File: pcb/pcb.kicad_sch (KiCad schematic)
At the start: 47 parts, among them J1 BATT, J2 BATT, SW1 SW_SPST, SW10 SW_SPST, SW11 SW_SPST, SW13 SW_SPST, SW14 SW_SPST, SW15 SW_SPST, SW16 SW_SPST, SW17 SW_SPST, SW19 SW_SPST, SW2 SW_SPST, SW20 SW_SPST, SW21 SW_SPST, SW3 SW_SPST, SW4 SW_SPST, SW5 SW_SPST, SW7 SW_SPST, SW8 SW_SPST, SW9 SW_SPST, U1 XIAO_nRF52840

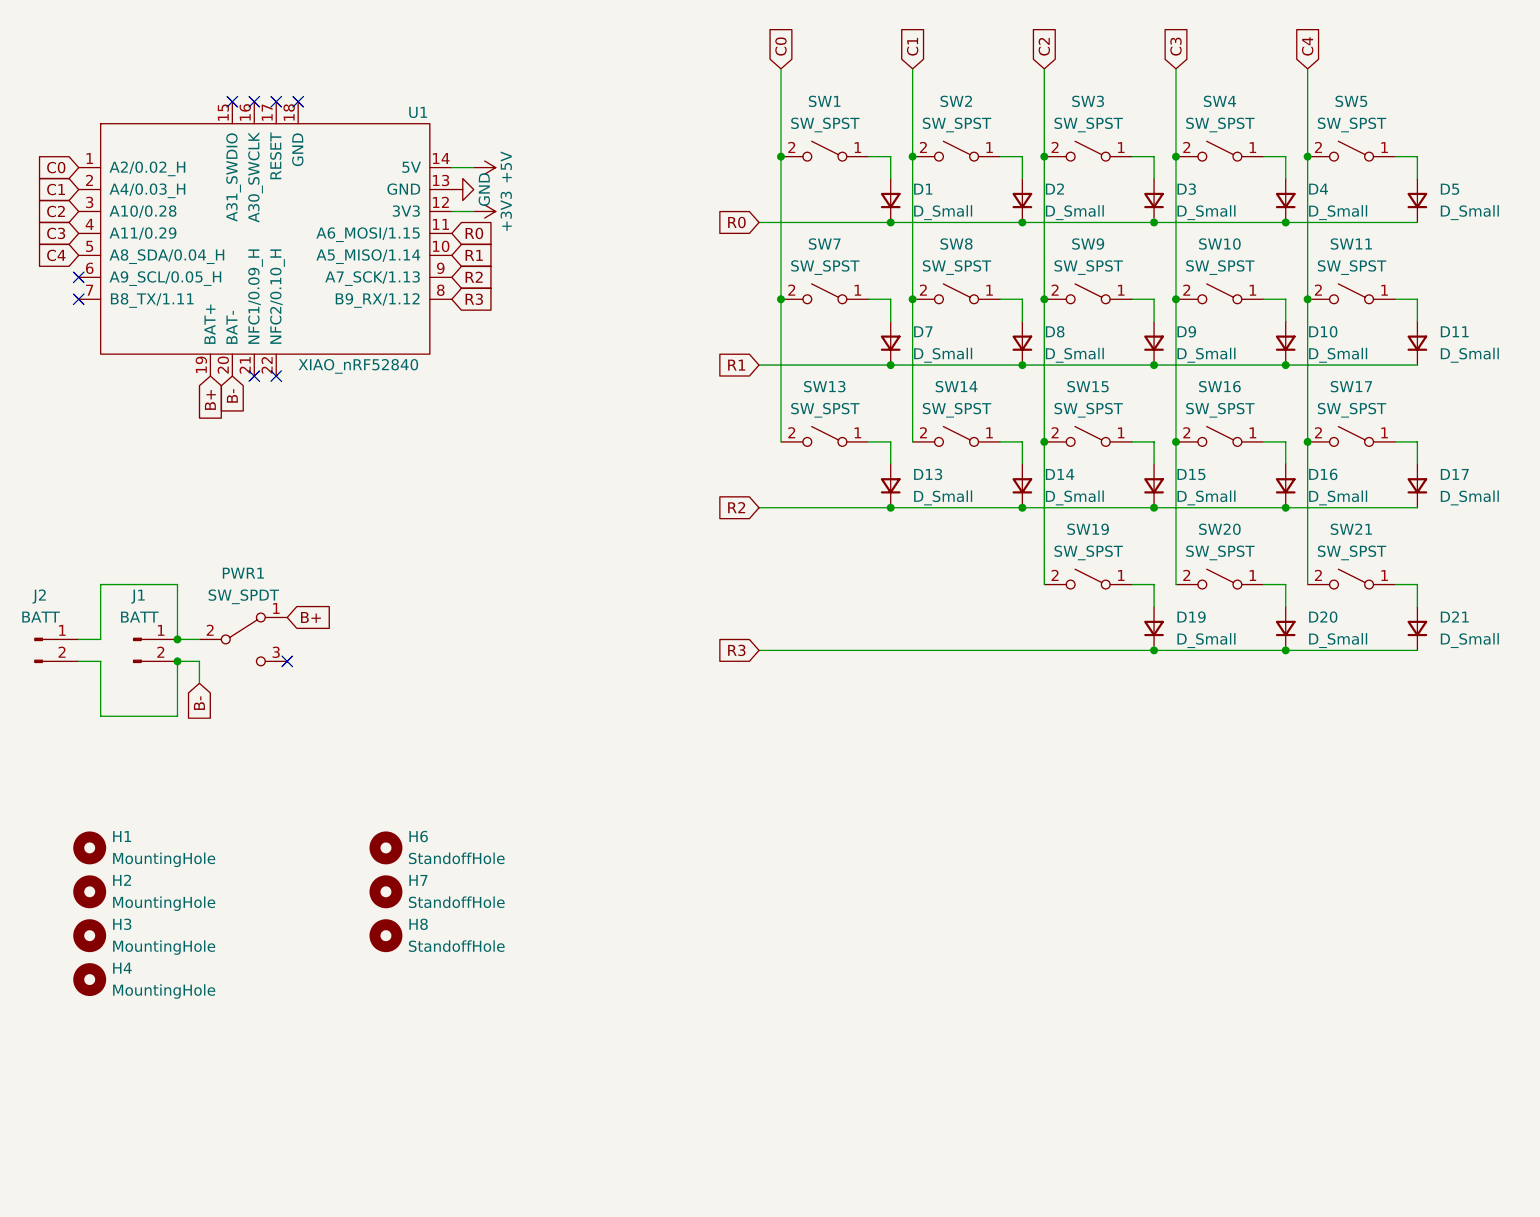
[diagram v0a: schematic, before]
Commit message: fix: symbol references
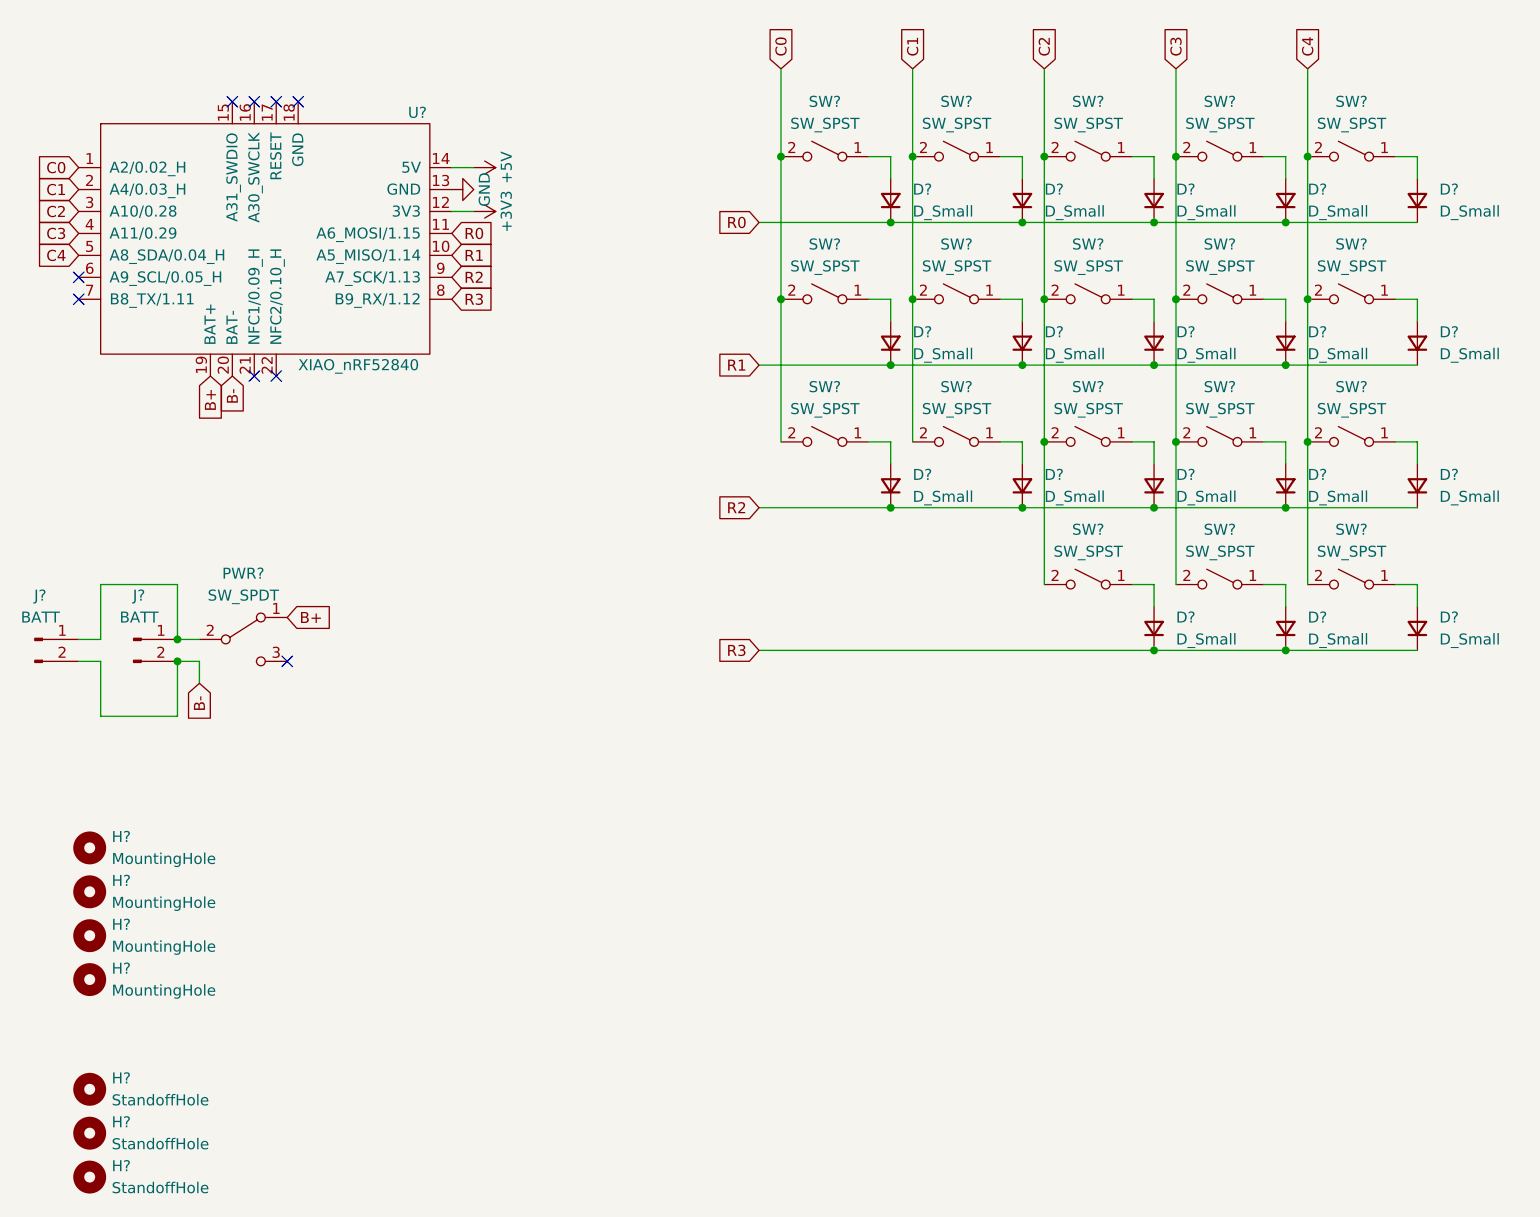
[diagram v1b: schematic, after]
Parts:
- renumbered D2 to D?, D19 to D?, D3 to D?, D13 to D?, D1 to D?, D4 to D?, D11 to D?, D7 to D?, D9 to D?, D16 to D?, D21 to D?, D8 to D?, D17 to D?, D15 to D?, D20 to D?, D10 to D?, D5 to D?, D14 to D?, H4 to H?, H6 to H?, H2 to H?, H3 to H?, H7 to H?, H1 to H?, H8 to H?, J1 to J?, J2 to J?, PWR1 to PWR?, SW17 to SW?, SW15 to SW?, SW9 to SW?, SW2 to SW?, SW21 to SW?, SW14 to SW?, SW3 to SW?, SW1 to SW?, SW11 to SW?, SW16 to SW?, SW7 to SW?, SW4 to SW?, SW8 to SW?, SW19 to SW?, SW13 to SW?, SW10 to SW?, SW20 to SW?, SW5 to SW?, U1 to U?
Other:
- moved on the sheet: H?

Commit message: add ci and 3d files
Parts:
- D? (x18): footprint scuffy:Diode_TH_SMD_DUAL -> one-s:Diode_TH_SMD_DUAL
- H? (x4): footprint scuffy:Hole_4.2mm -> one-s:Hole_4.2mm
- H? (x3): footprint scuffy:Hole_2.2mm -> one-s:Hole_2.2mm
- J?: footprint scuffy:Battery -> one-s:Battery
- J?: footprint scuffy:JST_SH_Battery_DUAL -> one-s:JST_SH_Battery_DUAL
- PWR?: footprint scuffy:MSK-12C02_DUAL -> one-s:MSK-12C02_DUAL
- SW? (x18): footprint scuffy:KS-27_KS-33_Hotswap_1U_DUAL -> one-s:KS-27_KS-33_Hotswap_1U_DUAL
- U?: footprint scuffy:XIAO_nRF52840_DUAL -> one-s:XIAO_nRF52840_DUAL

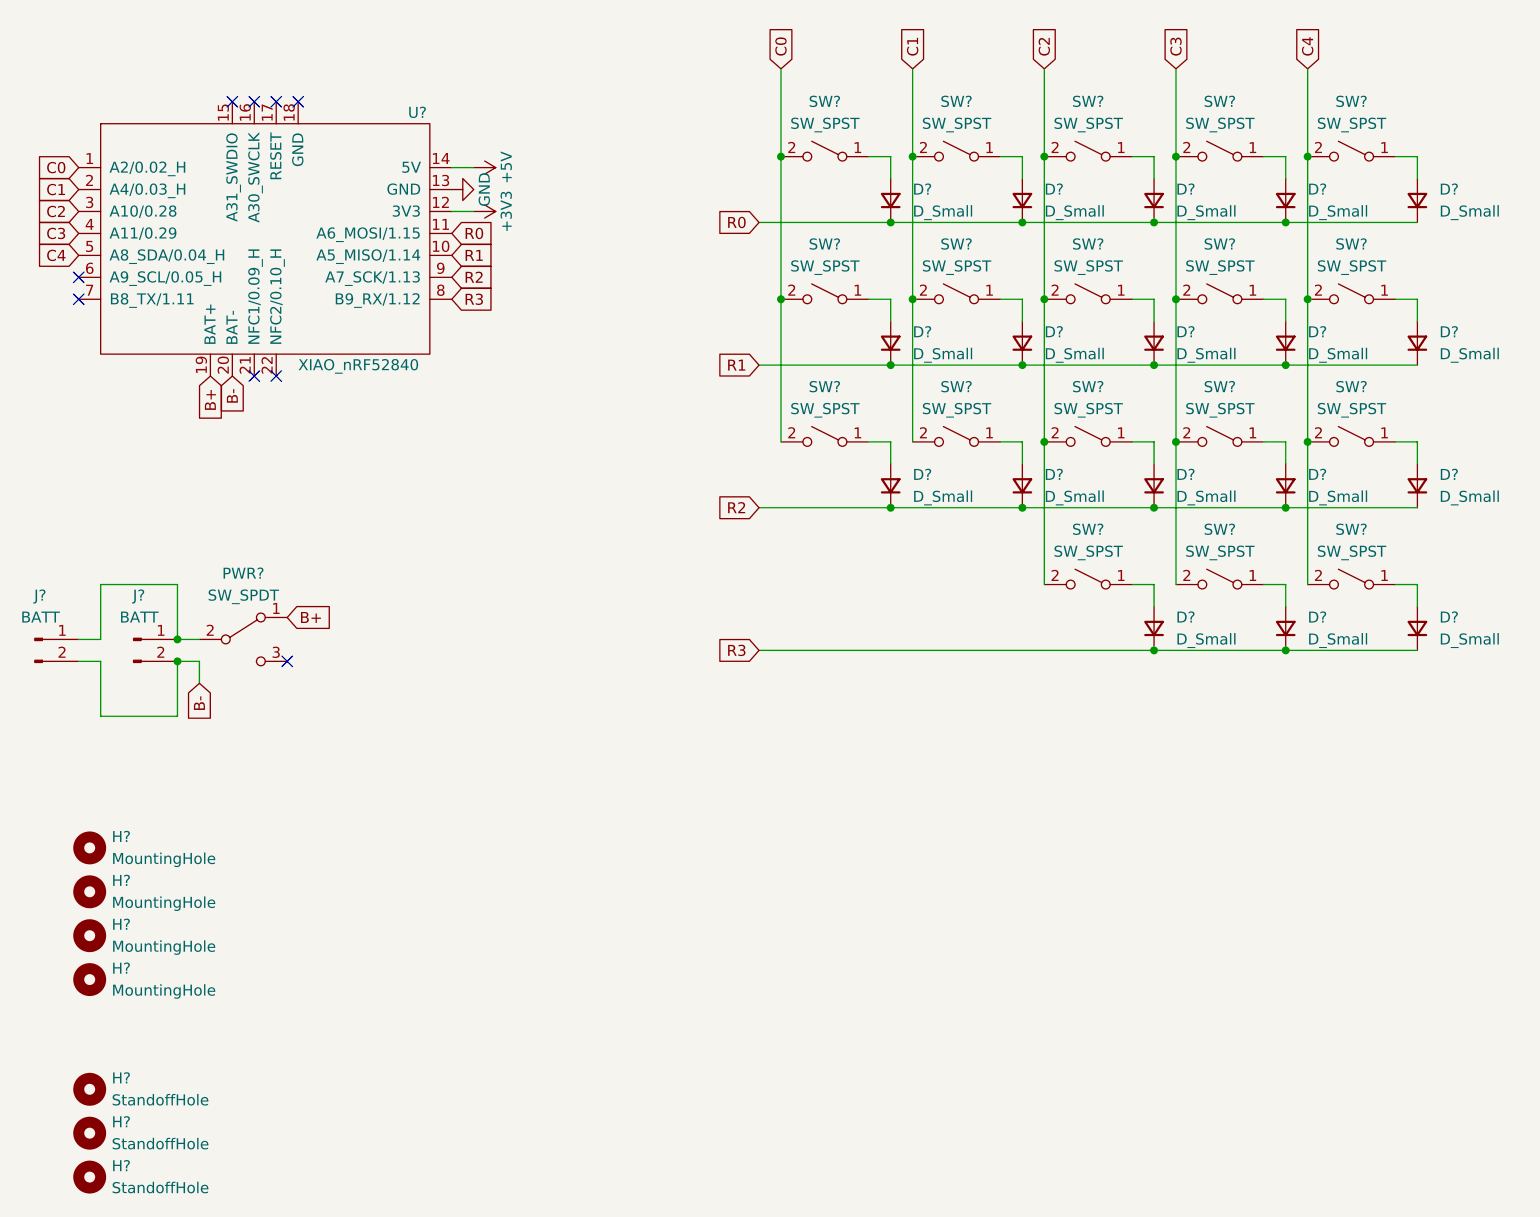
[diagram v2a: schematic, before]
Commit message: Modify PCB for Kailh P1316S
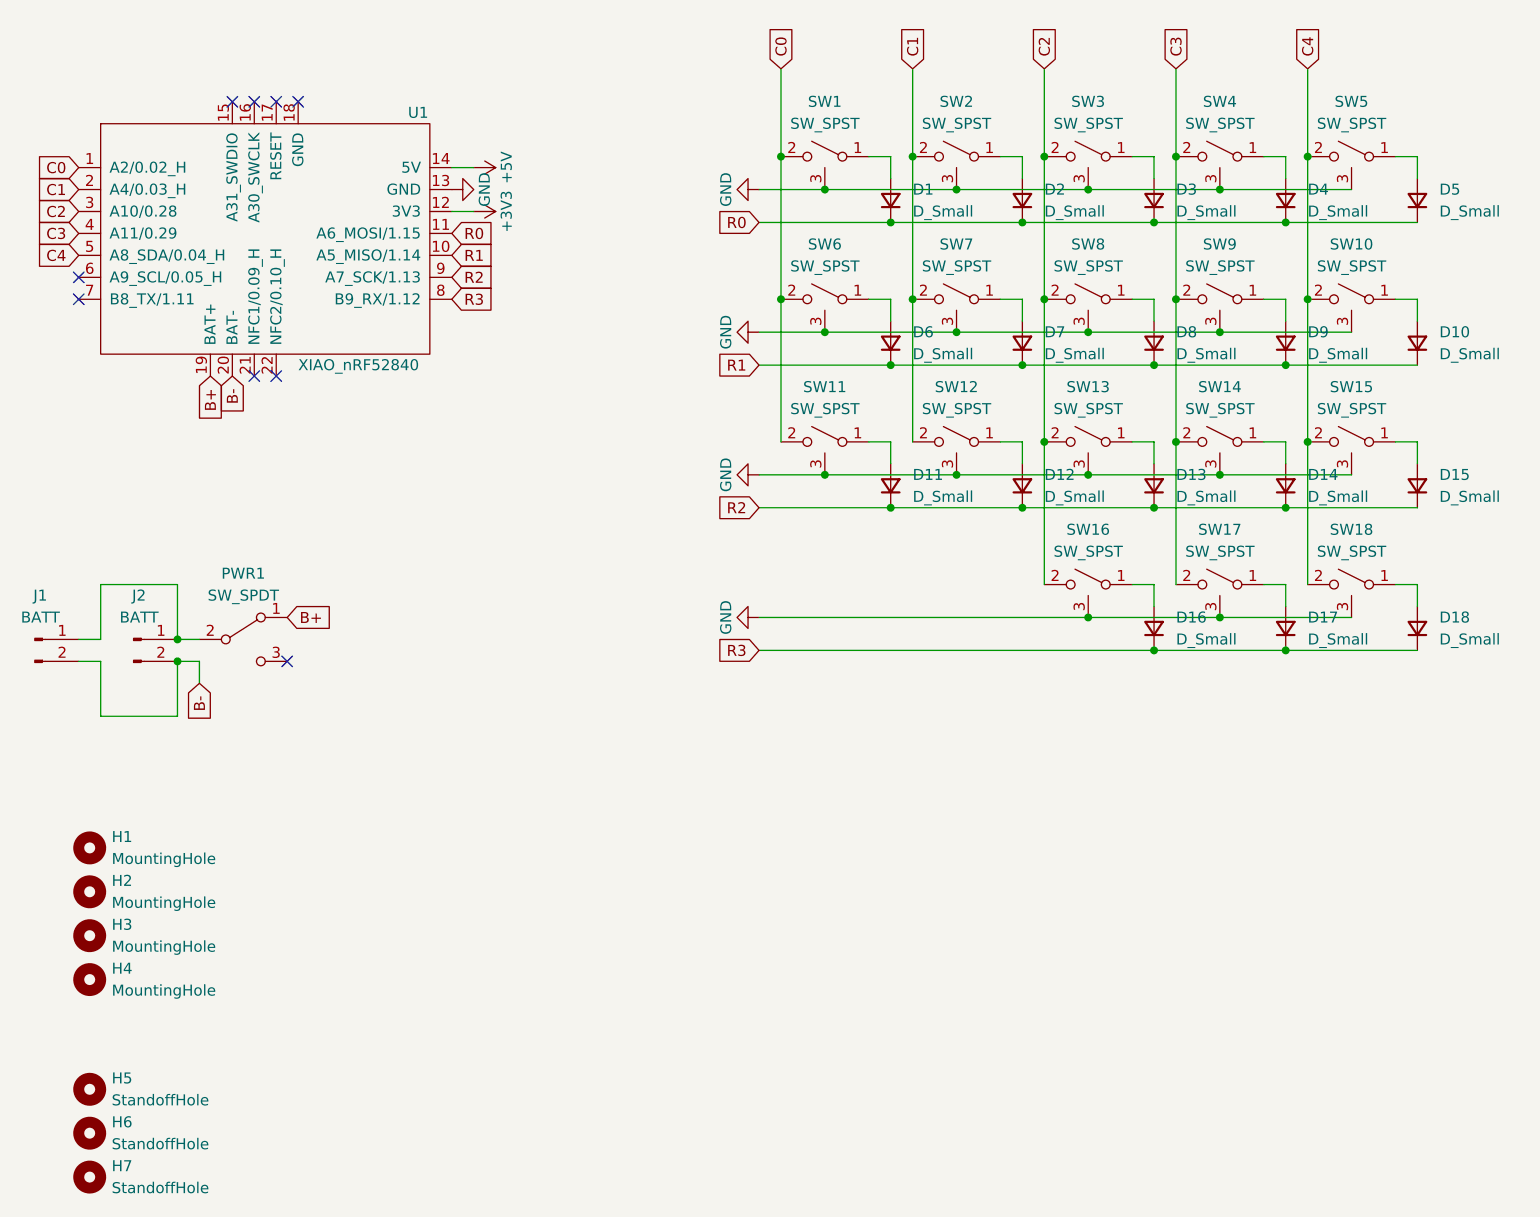
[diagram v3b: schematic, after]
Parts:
- SW1, SW10, SW11, SW12, SW13, SW14, SW15, SW16, SW17, SW18, SW2, SW3, SW4, SW5, SW6, SW7, SW8, SW9: renamed from SW?; footprint one-s:KS-27_KS-33_Hotswap_1U_DUAL -> one-s:CPG1316S01D02_REV; symbol Switch:SW_SPST -> one:SW_SPST_FRAME
- gave numbers to parts that had none: 29
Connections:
- net GND: now also SW1.3 (B), SW10.3 (B), SW11.3 (B), SW12.3 (B), SW13.3 (B), SW14.3 (B), SW15.3 (B), SW16.3 (B), SW17.3 (B), SW18.3 (B), SW2.3 (B), SW3.3 (B), SW4.3 (B), SW5.3 (B), SW6.3 (B), SW7.3 (B), SW8.3 (B), SW9.3 (B)
